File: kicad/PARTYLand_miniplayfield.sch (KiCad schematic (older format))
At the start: 18 parts, among them P1 CONN_6, U1 74HC595

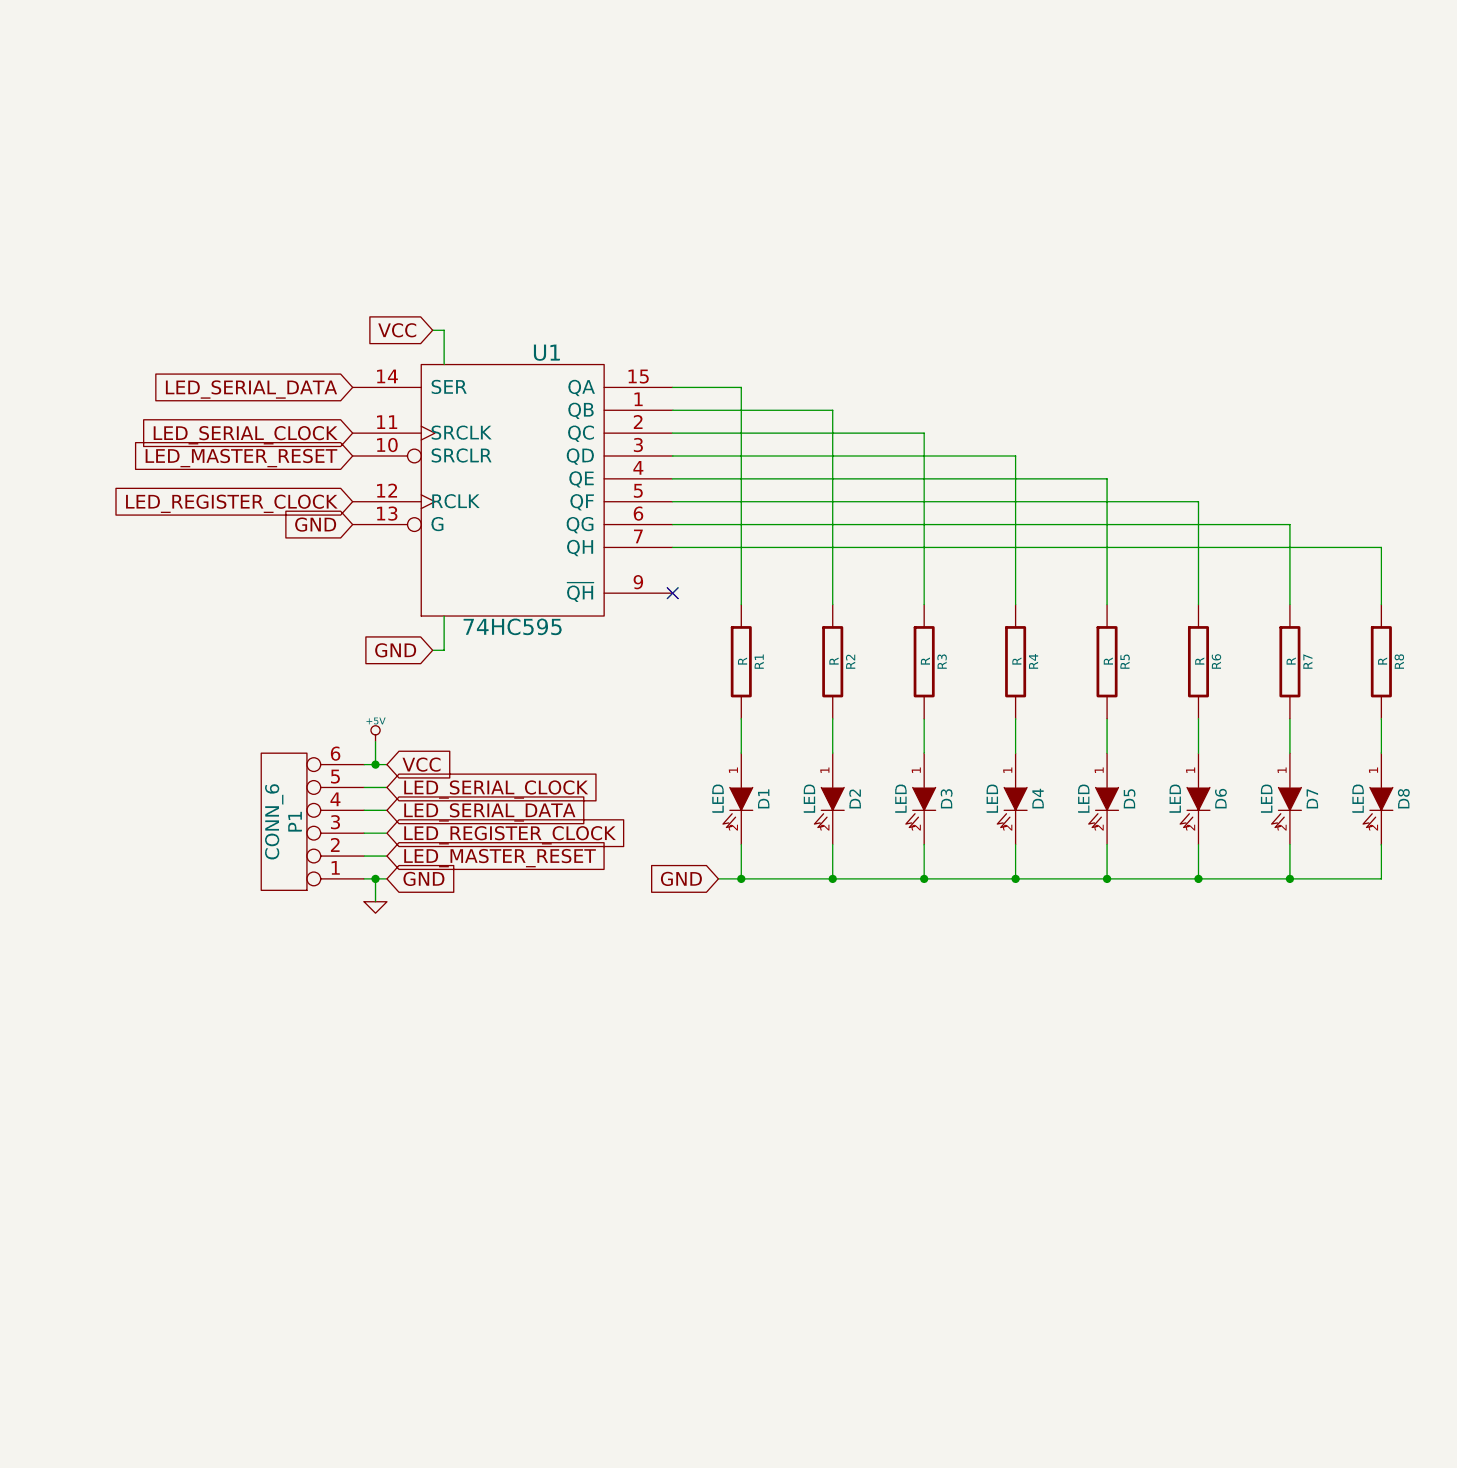
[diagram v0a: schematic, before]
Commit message: Added a second group of LEDs using a second daisychained shift register. WIP on positioning the footprints on the PCB
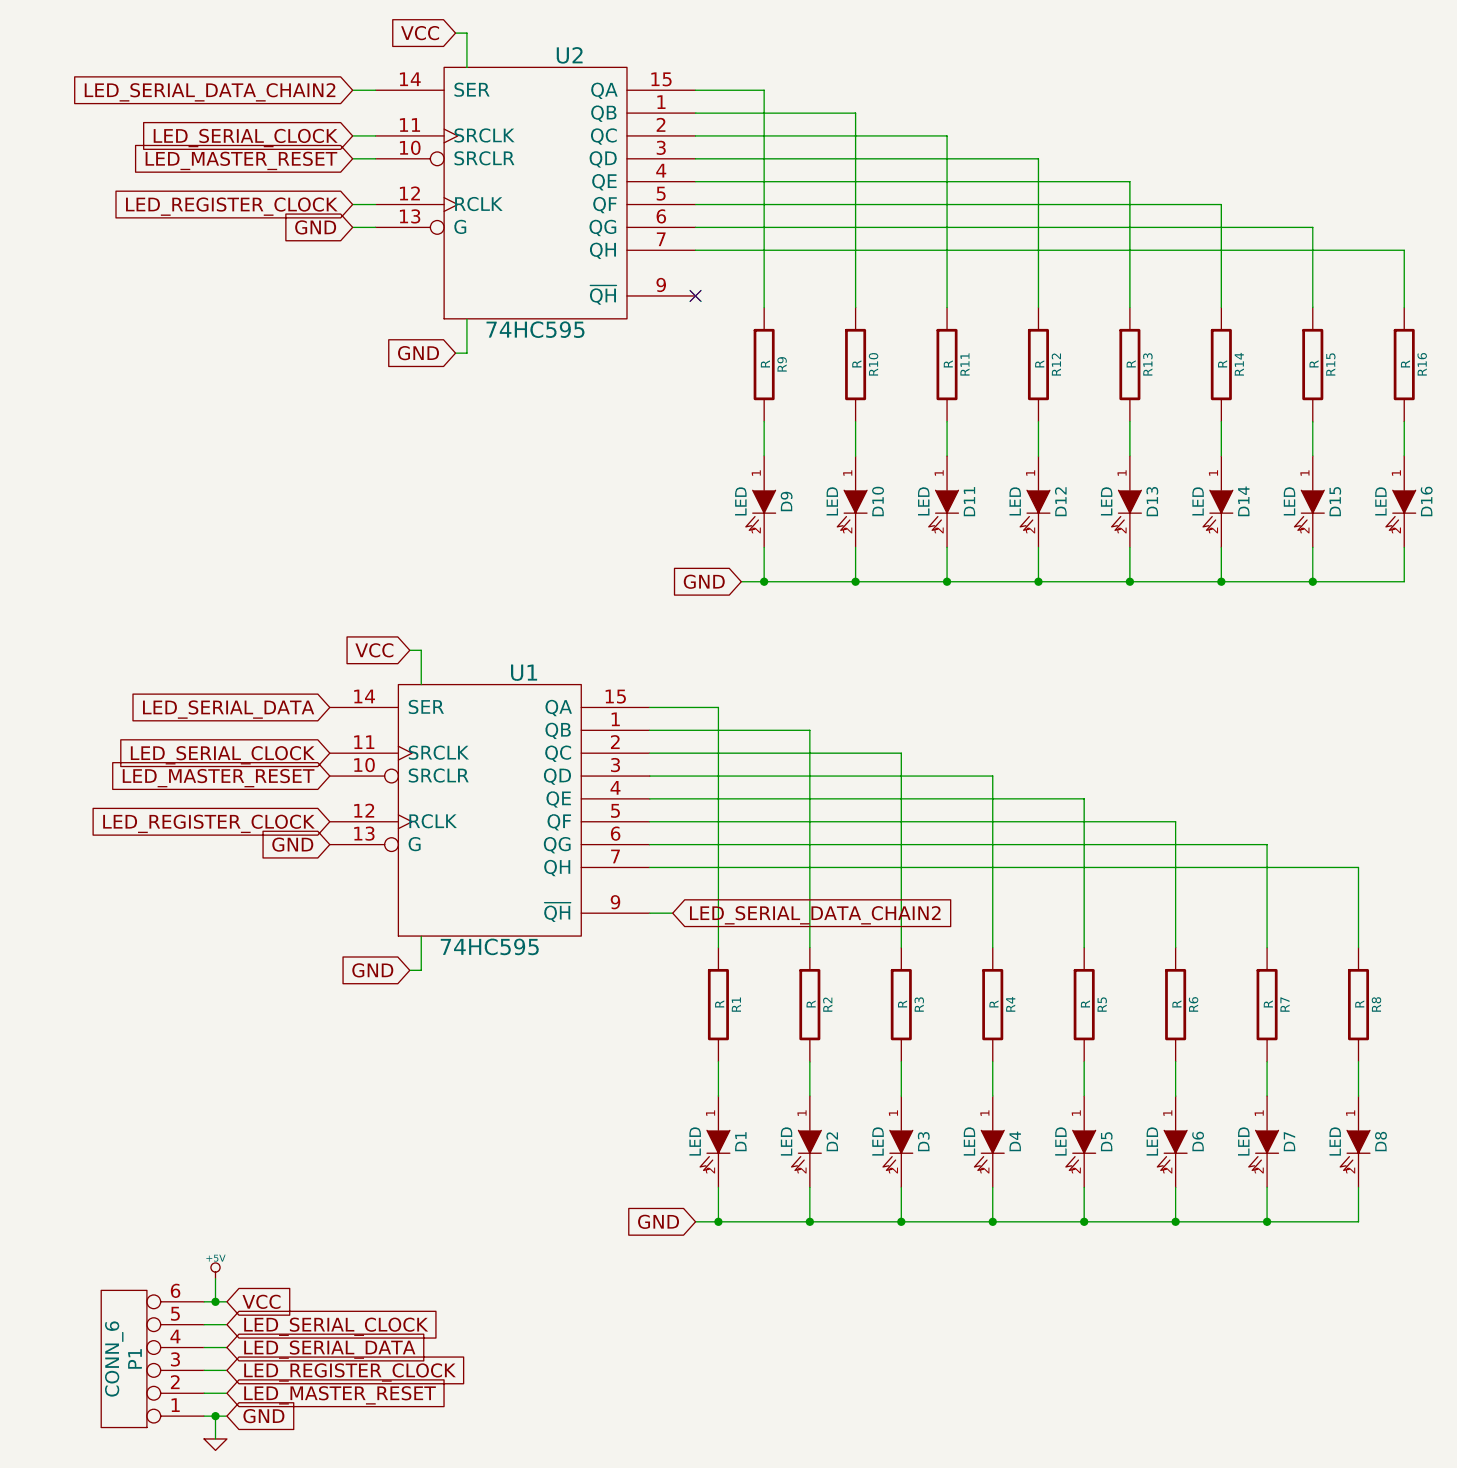
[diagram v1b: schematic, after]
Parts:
- added D10, D11, D12, D13, D14, D15, D16, D9: LED, LEDs:LED-3MM, symbol LED
- added R10, R11, R12, R13, R14, R15, R16, R9: R, Discret:R3, symbol R
- added U2: 74HC595, Sockets_DIP:DIP-16__300_ELL, symbol 74HC595
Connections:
- net +5V: now also U2.16 (VCC)
- net GND: now also D10.2 (K), D11.2 (K), D12.2 (K), D13.2 (K), D14.2 (K), D15.2 (K), D16.2 (K), D9.2 (K), U2.13 (G), U2.8 (GND)
- net LED_MASTER_RESET: now also U2.10 (SRCLR)
- net LED_REGISTER_CLOCK: now also U2.12 (RCLK)
- net LED_SERIAL_CLOCK: now also U2.11 (SRCLK)
- net LED_SERIAL_DATA_CHAIN2: now reaches U1.9 (~QH)
- net LED_SERIAL_DATA_CHAIN2: now also U2.14 (SER)
- new net: R10.1, U2.1 (QB)
- new net: R9.1, U2.15 (QA)
- new net: R11.1, U2.2 (QC)
- new net: R12.1, U2.3 (QD)
- new net: R13.1, U2.4 (QE)
- new net: R14.1, U2.5 (QF)
- new net: R15.1, U2.6 (QG)
- new net: R16.1, U2.7 (QH)
- new net: D12.1 (A), R12.2
- new net: D13.1 (A), R13.2
- new net: D14.1 (A), R14.2
- new net: D11.1 (A), R11.2
- new net: D10.1 (A), R10.2
- new net: D9.1 (A), R9.2
- new net: D15.1 (A), R15.2
- new net: D16.1 (A), R16.2
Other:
- moved on the sheet: D1, D2, D3, D4, D5, D6, D7, D8, P1, R1, R2, R3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

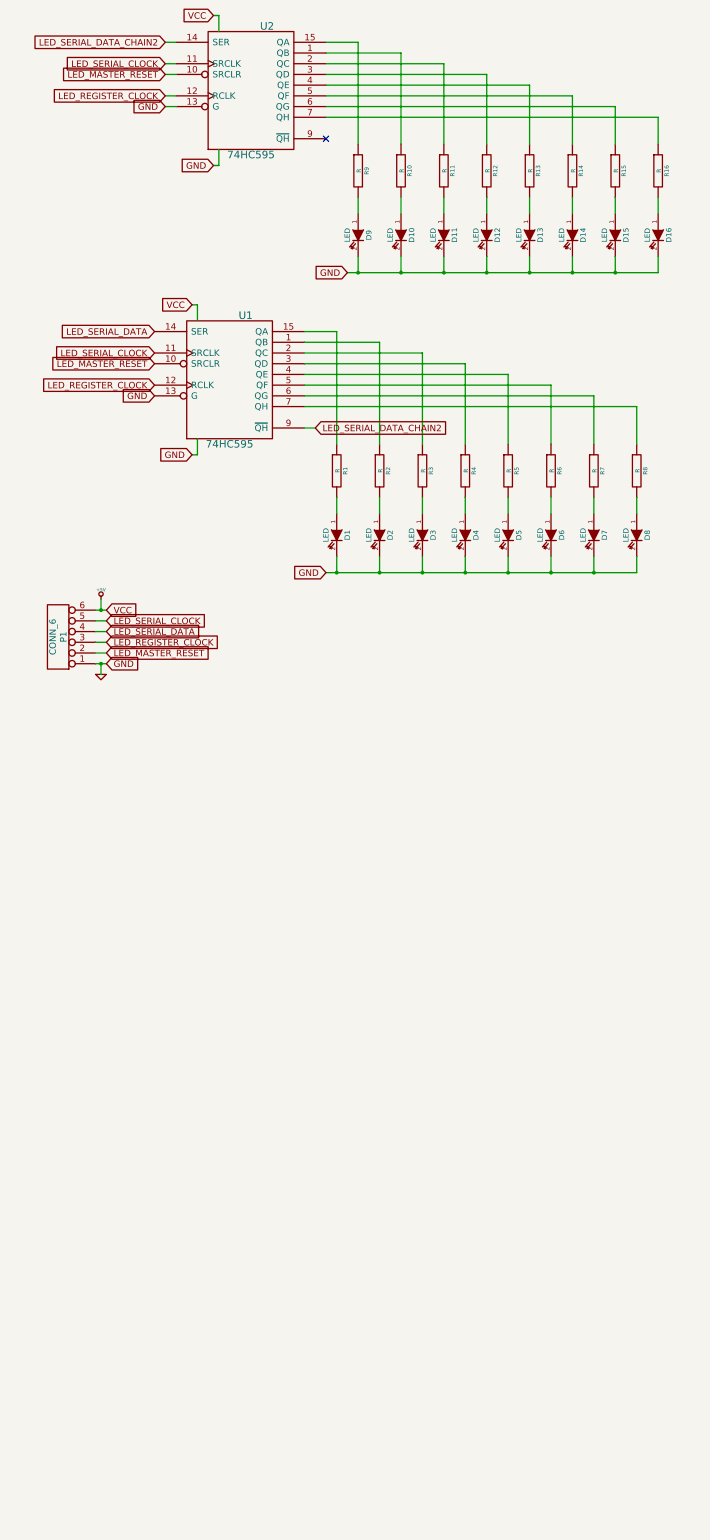
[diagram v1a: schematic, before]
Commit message: Adding more LED circuitry to the PARTYLand miniplayfield.
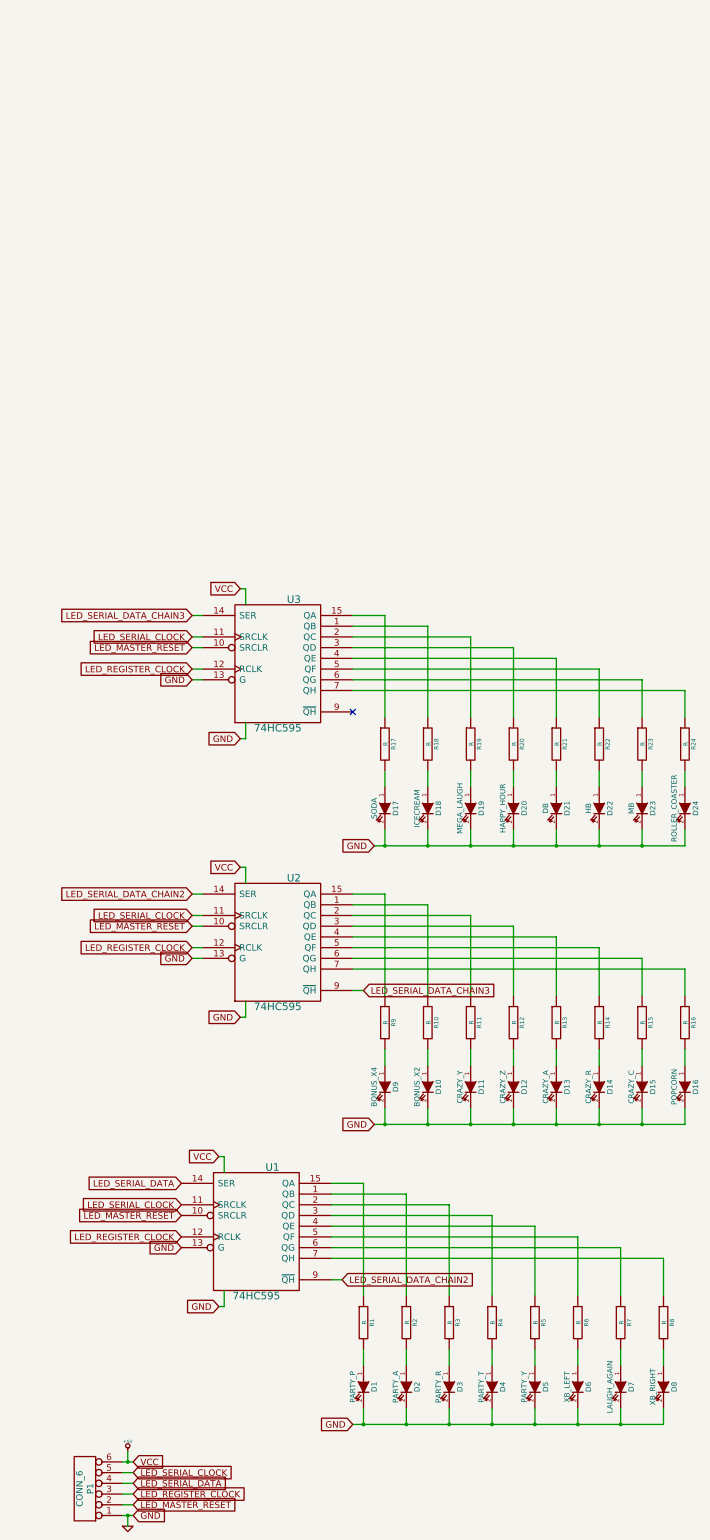
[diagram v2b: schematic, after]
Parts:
- added D17: SODA, LEDs:LED-3MM, symbol LED
- added D18: ICECREAM, LEDs:LED-3MM, symbol LED
- added D19: MEGA_LAUGH, LEDs:LED-3MM, symbol LED
- added D20: HAPPY_HOUR, LEDs:LED-3MM, symbol LED
- added D21: DB, LEDs:LED-3MM, symbol LED
- added D22: HB, LEDs:LED-3MM, symbol LED
- added D23: MB, LEDs:LED-3MM, symbol LED
- added D24: ROLLER_COASTER, LEDs:LED-3MM, symbol LED
- added R17, R18, R19, R20, R21, R22, R23, R24: R, Discret:R3, symbol R
- added U3: 74HC595, Sockets_DIP:DIP-16__300_ELL, symbol 74HC595
- D1: value LED -> PARTY_P
- D10: value LED -> BONUS_X2
- D11: value LED -> CRAZY_Y
- D12: value LED -> CRAZY_Z
- D13: value LED -> CRAZY_A
- D14: value LED -> CRAZY_R
- D15: value LED -> CRAZY_C
- D16: value LED -> POPCORN
- D2: value LED -> PARTY_A
- D3: value LED -> PARTY_R
- D4: value LED -> PARTY_T
- D5: value LED -> PARTY_Y
- D6: value LED -> XB_LEFT
- D7: value LED -> LAUGH_AGAIN
- D8: value LED -> XB_RIGHT
- D9: value LED -> BONUS_X4
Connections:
- net +5V: now also U3.16 (VCC)
- net GND: now also D17.2 (K), D18.2 (K), D19.2 (K), D20.2 (K), D21.2 (K), D22.2 (K), D23.2 (K), D24.2 (K), U3.13 (G), U3.8 (GND)
- net LED_MASTER_RESET: now also U3.10 (SRCLR)
- net LED_REGISTER_CLOCK: now also U3.12 (RCLK)
- net LED_SERIAL_CLOCK: now also U3.11 (SRCLK)
- net LED_SERIAL_DATA_CHAIN3: now reaches U2.9 (~QH)
- net LED_SERIAL_DATA_CHAIN3: now also U3.14 (SER)
- new net: R18.1, U3.1 (QB)
- new net: R17.1, U3.15 (QA)
- new net: R19.1, U3.2 (QC)
- new net: R20.1, U3.3 (QD)
- new net: R21.1, U3.4 (QE)
- new net: R22.1, U3.5 (QF)
- new net: R23.1, U3.6 (QG)
- new net: R24.1, U3.7 (QH)
- new net: D20.1 (A), R20.2
- new net: D21.1 (A), R21.2
- new net: D22.1 (A), R22.2
- new net: D19.1 (A), R19.2
- new net: D18.1 (A), R18.2
- new net: D17.1 (A), R17.2
- new net: D23.1 (A), R23.2
- new net: D24.1 (A), R24.2
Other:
- moved on the sheet: D1, D10, D11, D12, D13, D14, D15, D16, D2, D3, D4, D5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

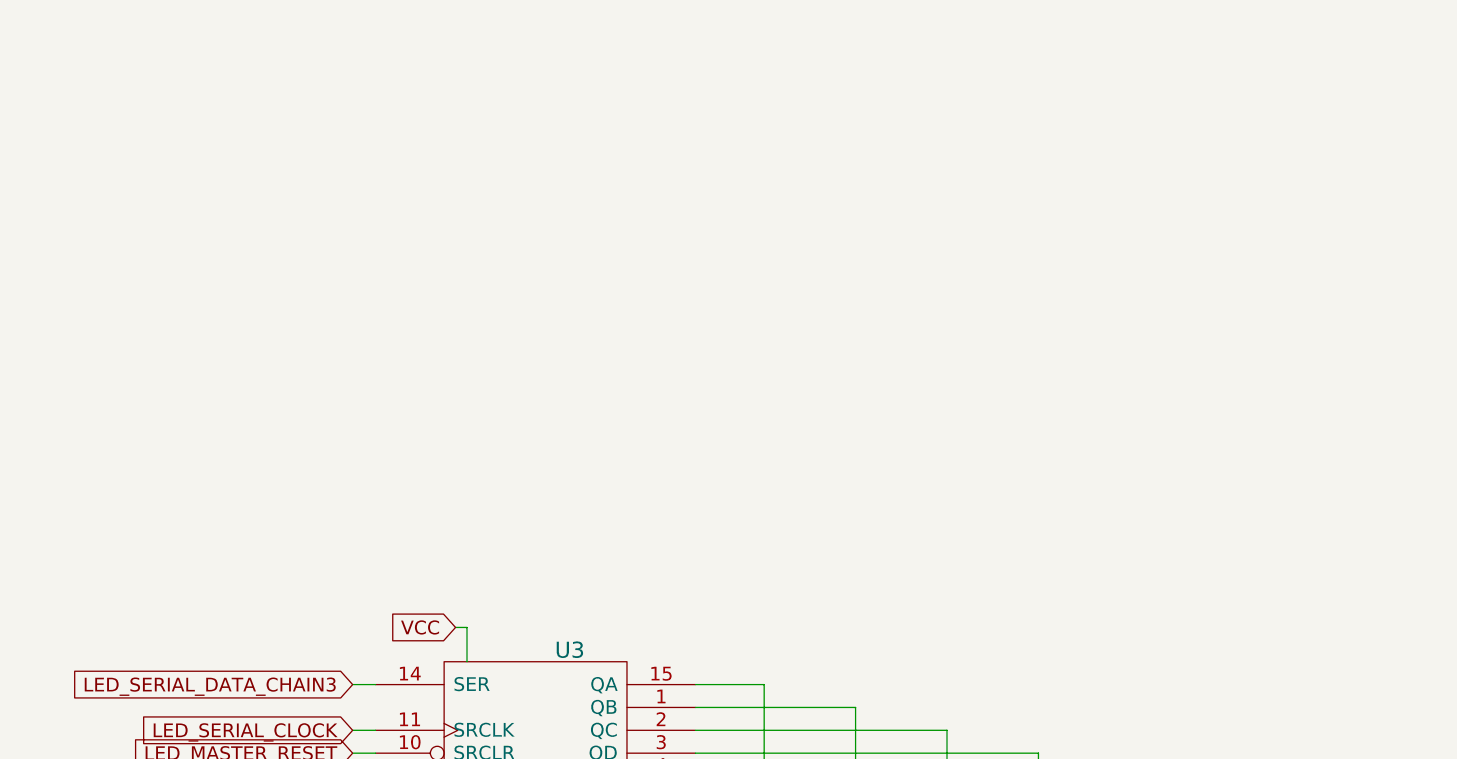
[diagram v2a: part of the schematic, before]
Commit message: A few more LEDs in the PARTYLand mini-playfield PCB.
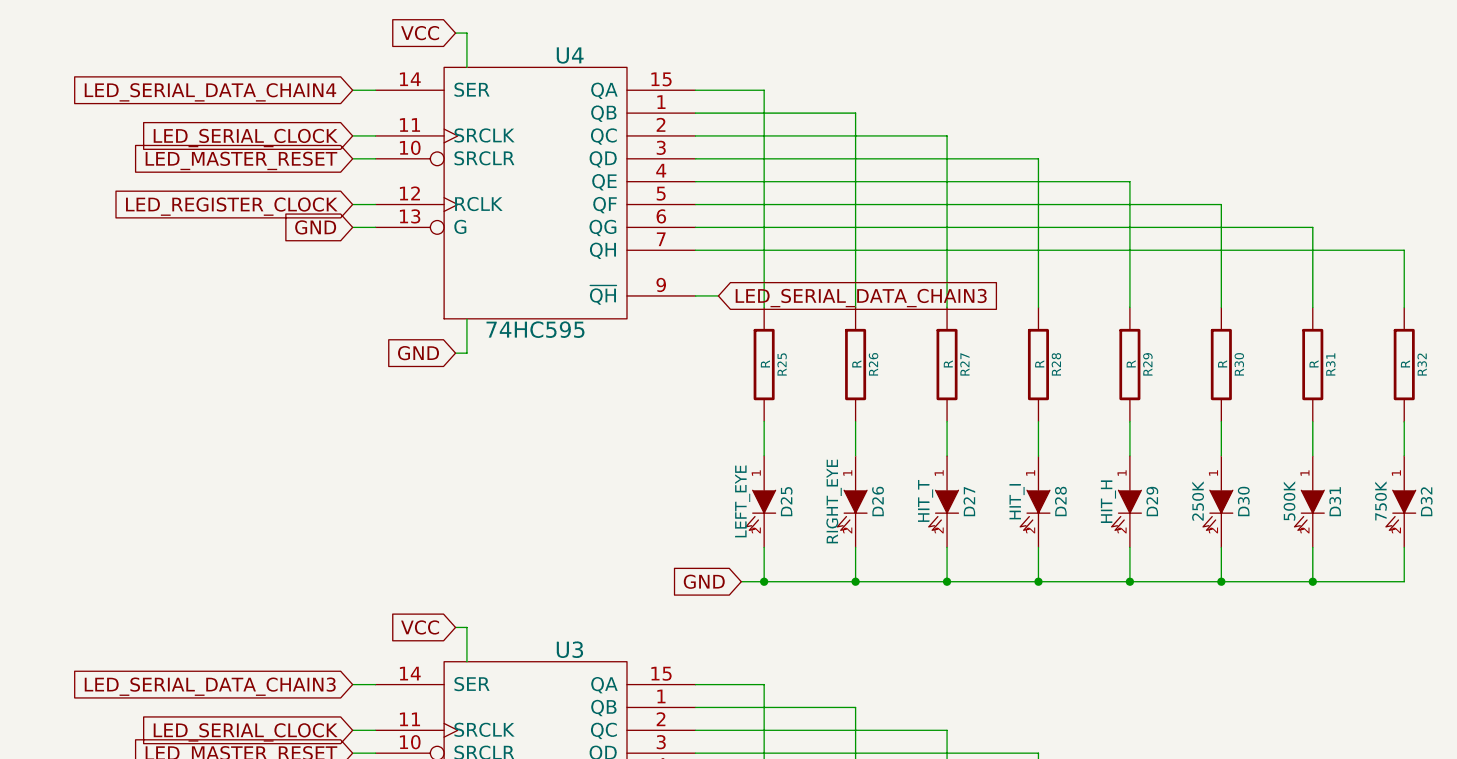
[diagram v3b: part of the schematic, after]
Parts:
- added D25: LEFT_EYE, LEDs:LED-3MM, symbol LED
- added D26: RIGHT_EYE, LEDs:LED-3MM, symbol LED
- added D27: HIT_T, LEDs:LED-3MM, symbol LED
- added D28: HIT_I, LEDs:LED-3MM, symbol LED
- added D29: HIT_H, LEDs:LED-3MM, symbol LED
- added D30: 250K, LEDs:LED-3MM, symbol LED
- added D31: 500K, LEDs:LED-3MM, symbol LED
- added D32: 750K, LEDs:LED-3MM, symbol LED
- added R25, R26, R27, R28, R29, R30, R31, R32: R, Discret:R3, symbol R
- added U4: 74HC595, Sockets_DIP:DIP-16__300_ELL, symbol 74HC595
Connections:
- net +5V: now also U4.16 (VCC)
- net GND: now also D25.2 (K), D26.2 (K), D27.2 (K), D28.2 (K), D29.2 (K), D30.2 (K), D31.2 (K), D32.2 (K), U4.13 (G), U4.8 (GND)
- net LED_MASTER_RESET: now also U4.10 (SRCLR)
- net LED_REGISTER_CLOCK: now also U4.12 (RCLK)
- net LED_SERIAL_CLOCK: now also U4.11 (SRCLK)
- net LED_SERIAL_DATA_CHAIN3: now also U4.9 (~QH)
- new net: R26.1, U4.1 (QB)
- new net: R25.1, U4.15 (QA)
- new net: R27.1, U4.2 (QC)
- new net: R28.1, U4.3 (QD)
- new net: R29.1, U4.4 (QE)
- new net: R30.1, U4.5 (QF)
- new net: R31.1, U4.6 (QG)
- new net: R32.1, U4.7 (QH)
- new net: D28.1 (A), R28.2
- new net: D29.1 (A), R29.2
- new net: D30.1 (A), R30.2
- new net: D27.1 (A), R27.2
- new net: D26.1 (A), R26.2
- new net: D25.1 (A), R25.2
- new net: D31.1 (A), R31.2
- new net: D32.1 (A), R32.2
- new net LED_SERIAL_DATA_CHAIN4: U4.14 (SER)
